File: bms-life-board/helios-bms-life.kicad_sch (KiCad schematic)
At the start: 66 parts, among them J1 Debug, J2 Output, J3 Outboard, J4 Battery, Q1 NMOS, Q2 SSM3J332R, U1 TPSM861253, U2 STM32L011F4Ux, U3 TPS22811, U4 TPS563207s, U5 BQ25306, U6 THVD1400D

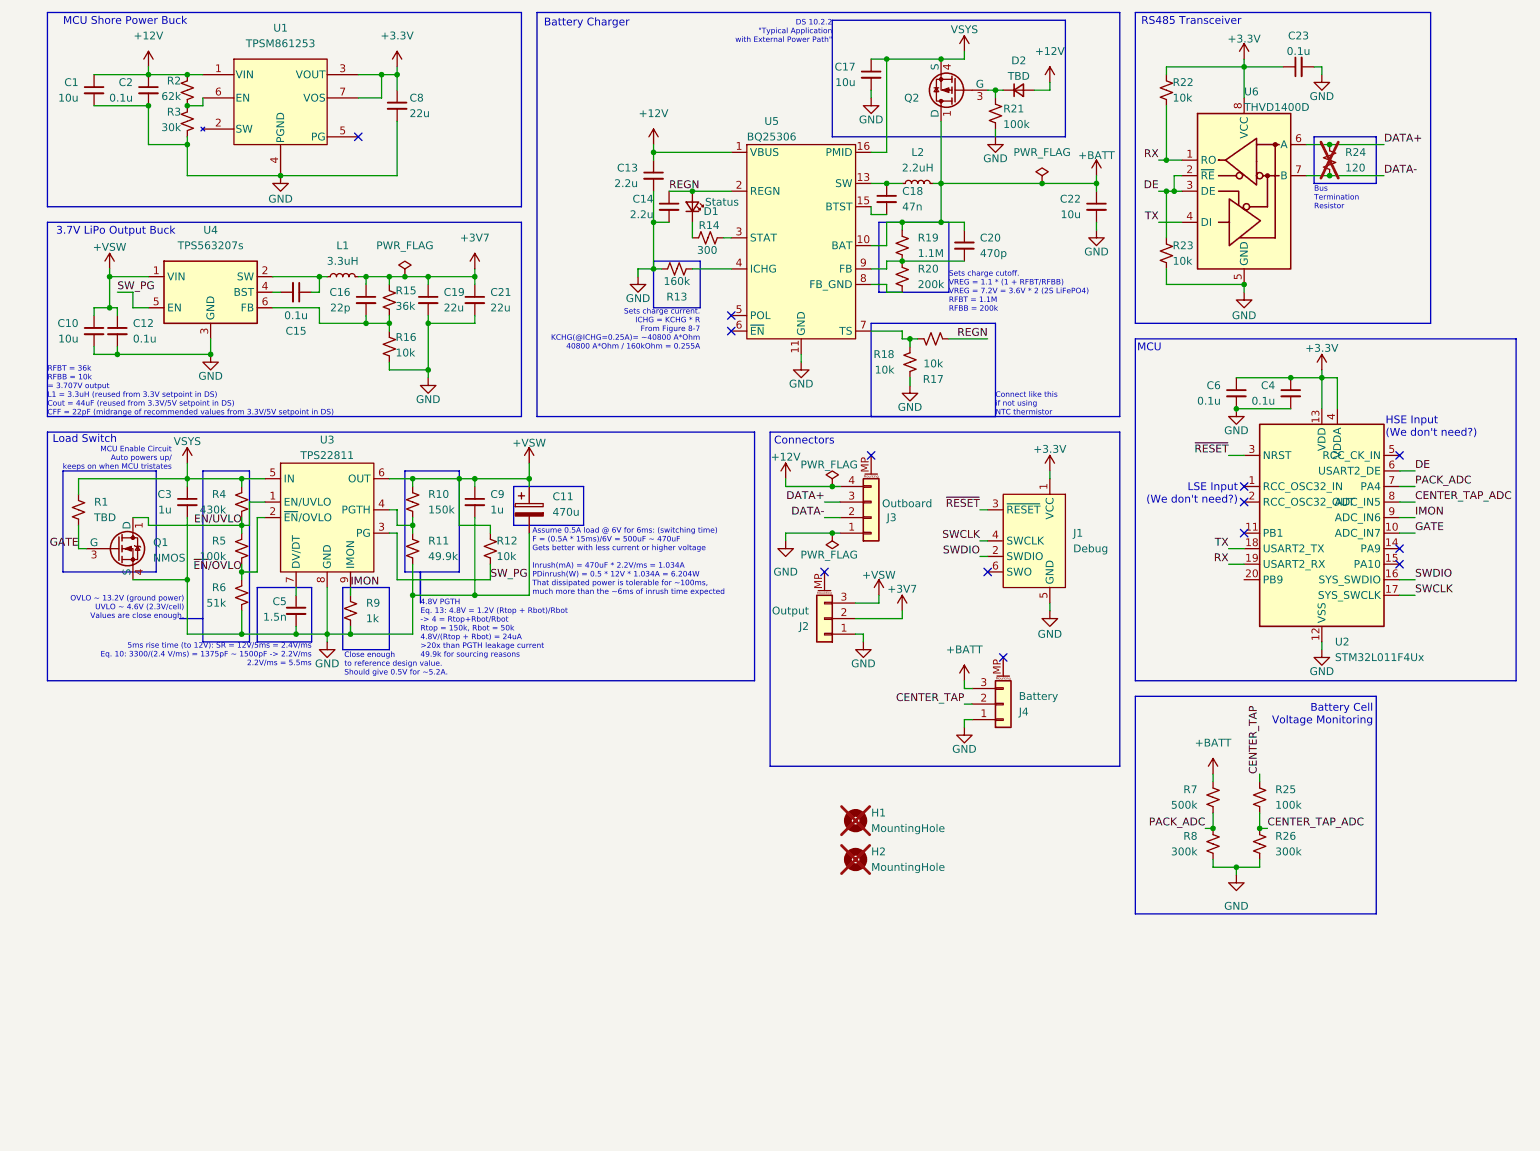
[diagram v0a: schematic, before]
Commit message: post DR LiFe board partially done, need to clean up the BoM on digikey BADDD
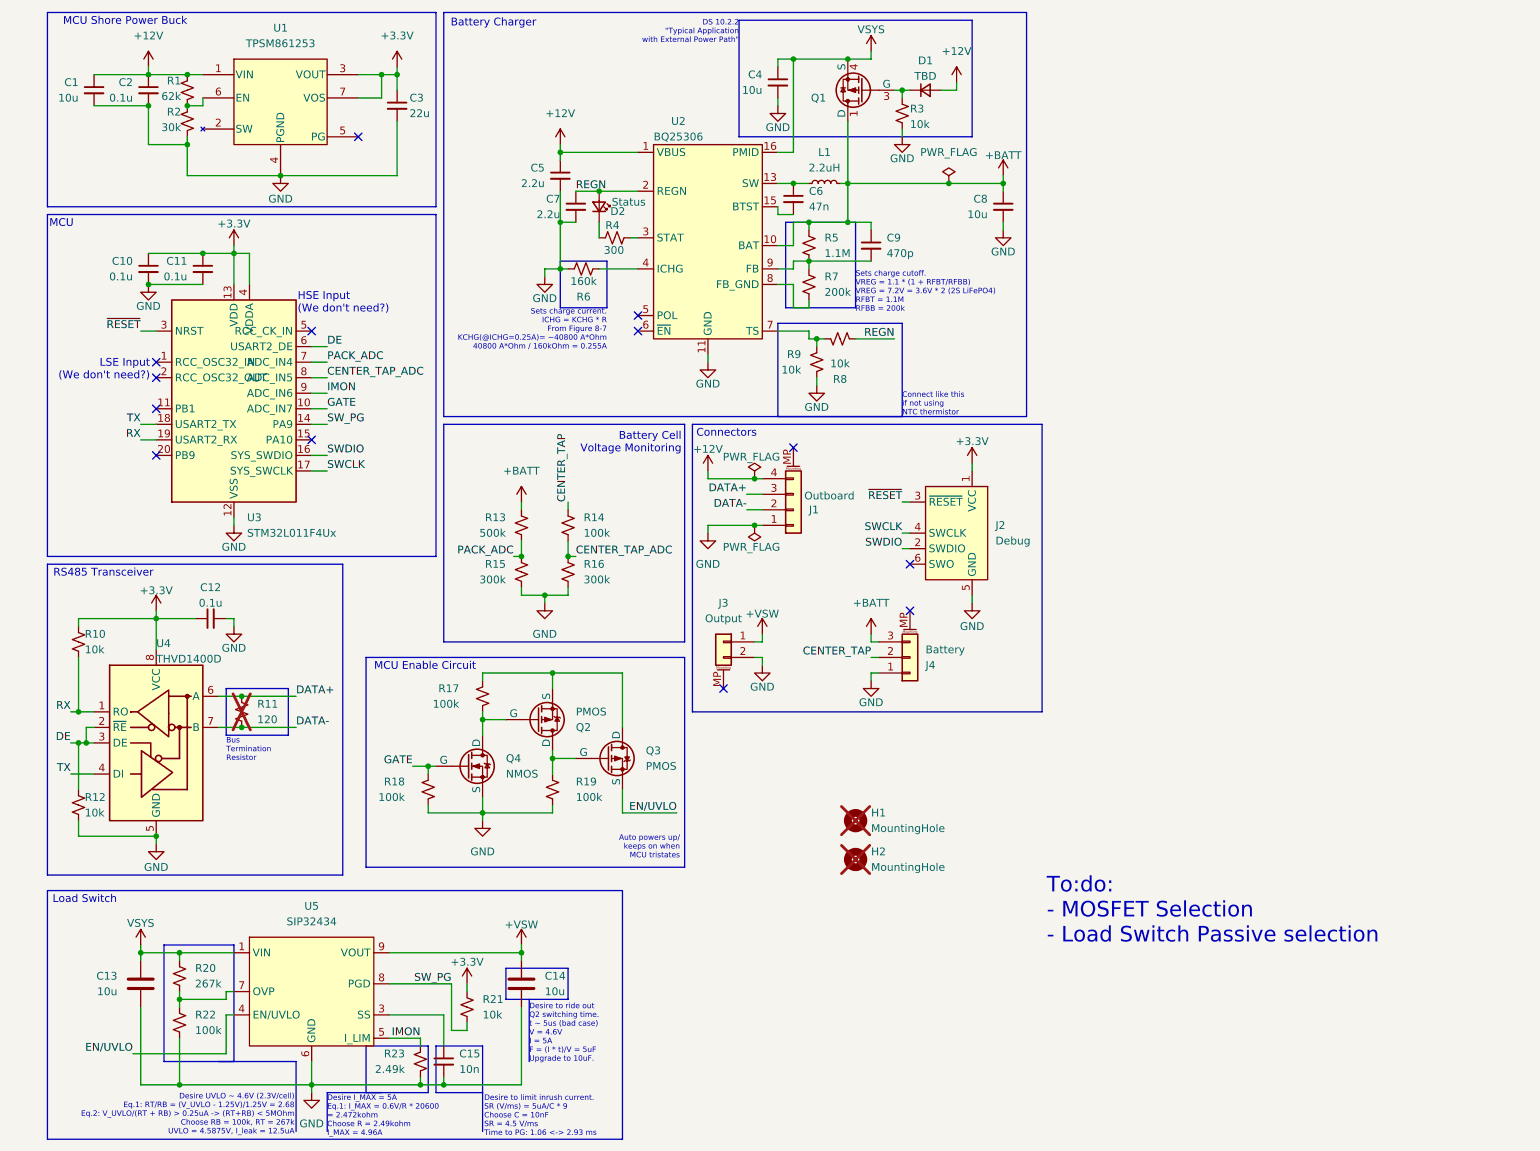
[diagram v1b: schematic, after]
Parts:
- removed C10: 10u, Capacitor_SMD:C_0603_1608Metric, symbol Device:C_Small
- removed C11: 470u, Capacitor_THT:CP_Radial_D6.3mm_P2.50mm, symbol Device:C_Polarized
- removed C12: 0.1u, Capacitor_SMD:C_0402_1005Metric, symbol Device:C_Small
- removed C16: 22p, Capacitor_SMD:C_0402_1005Metric, symbol Device:C_Small
- removed C19, C21: 22u, Capacitor_SMD:C_0603_1608Metric, symbol Device:C_Small
- removed C3, C9: 1u, Capacitor_SMD:C_0402_1005Metric, symbol Device:C_Small
- removed C5: 1.5n, Capacitor_SMD:C_0402_1005Metric, symbol Device:C_Small
- removed J2: Output, Connector_JST:JST_ZE_SM03B-ZESS-TB_1x03-1MP_P1.50mm_Horizontal, symbol Connector_Generic_MountingPin:Conn_01x03_MountingPin
- removed L1: 3.3uH, Inductor_SMD:L_1008_2520Metric, symbol Device:L_Small
- removed Q1: NMOS, Helios-BMS:SOT-1220_UDFN6B_TOS-L, symbol Helios-BMS:SSM6K388NU
- removed R1: TBD, Resistor_SMD:R_0402_1005Metric, symbol Device:R_Small_US
- removed R10: 150k, Resistor_SMD:R_0402_1005Metric, symbol Device:R_Small_US
- removed R11: 49.9k, Resistor_SMD:R_0402_1005Metric, symbol Device:R_Small_US
- removed R12, R16: 10k, Resistor_SMD:R_0402_1005Metric, symbol Device:R_Small_US
- removed R15: 36k, Resistor_SMD:R_0402_1005Metric, symbol Device:R_Small_US
- removed R4: 430k, Resistor_SMD:R_0402_1005Metric, symbol Device:R_Small_US
- removed R5: 100k, Resistor_SMD:R_0402_1005Metric, symbol Device:R_Small_US
- removed R6: 51k, Resistor_SMD:R_0402_1005Metric, symbol Device:R_Small_US
- removed R9: 1k, Resistor_SMD:R_0402_1005Metric, symbol Device:R_Small_US
- removed U3: TPS22811, Helios-BMS:TPS22811, symbol Helios-BMS:TPS22811
- removed U4: TPS563207s, Package_TO_SOT_SMD:SOT-563, symbol Regulator_Switching:TPS563206
- added C13, C14: 10u, Capacitor_SMD:C_0603_1608Metric, symbol Device:C
- added J3: Output, Connector_JST:JST_ZE_SM02B-ZESS-TB_1x02-1MP_P1.50mm_Horizontal, symbol Connector_Generic_MountingPin:Conn_01x02_MountingPin
- added Q2, Q3: PMOS, symbol Simulation_SPICE:PMOS
- added Q4: NMOS, symbol Simulation_SPICE:NMOS
- added R17, R18, R19, R22: 100k, Resistor_SMD:R_0402_1005Metric, symbol Device:R_Small_US
- added R20: 267k, Resistor_SMD:R_0402_1005Metric, symbol Device:R_Small_US
- added R21: 10k, Resistor_SMD:R_0402_1005Metric, symbol Device:R_Small_US
- added R23: 2.49k, Resistor_SMD:R_0402_1005Metric, symbol Device:R_Small_US
- added U5: SIP32434, Package_DFN_QFN:Maxim_TDFN-10-1EP_3x3mm_P0.5mm_EP1.58x2.35mm, symbol Helios-BMS:SIP32434
- C15: value 0.1u -> 10n
- R3: renamed from R21; value 100k -> 10k
- renumbered C6 to C10, C4 to C11, C23 to C12, C8 to C3, C17 to C4, C13 to C5, C18 to C6, C14 to C7, C22 to C8, C20 to C9, D2 to D1, D1 to D2, J3 to J1, J1 to J2, L2 to L1, Q2 to Q1, R2 to R1, R22 to R10, R24 to R11, R23 to R12, R7 to R13, R25 to R14, R8 to R15, R26 to R16, R3 to R2, R14 to R4, R19 to R5, R13 to R6, R20 to R7, R17 to R8, R18 to R9, U5 to U2, U2 to U3, U6 to U4
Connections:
- net +3.3V: now also R21.2
- net +VSW: now also C14.1, J3.1 (Pin_1), U5.10 (VOUT), U5.9 (VOUT)
- net EN/UVLO: now also Q3.3 (S), U5.4 (EN/UVLO)
- net GATE: now also Q4.2 (G), R18.1
- net GND: now also C15.2, C13.2, C14.2, J3.2 (Pin_2), Q4.3 (S), R18.2, R19.2, R22.1, R23.1, U5.11 (GND), U5.6 (GND)
- net IMON: now also R23.2, U5.5 (I_LIM)
- net SW_PG: now also U3.14 (PA9), R21.1, U5.8 (PGD)
- net at C15.1: now also U5.3 (SS)
- net VSYS renamed VIN
- net VIN: now also C13.1, R20.2, U5.1 (VIN), U5.2 (VIN)
- new net: Q2.1 (D), Q3.2 (G), R19.1
- new net: Q2.2 (G), Q4.1 (D), R17.2
- new net: Q2.3 (S), Q3.1 (D), R17.1
- new net: R20.1, R22.2, U5.7 (OVP)
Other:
- note added: "Auto powers up/ keeps on when MCU tristates"
- note added: "Desire I_MAX = 5A Eq.1: I_MAX = 0.6V/R * 20600 = 2.472kohm Choose R = 2.49kohm I_MAX = 4.96A"
- note added: "Desire UVLO ~ 4.6V (2.3V/cell) Eq.1: RT/RB = (V_UVLO - 1.25V)/1.25V = 2.68 Eq.2: V_UVLO/(RT + RB) > 0.25uA -> (RT+RB) < 5MOhm Choose RB = 100k, RT = 267k UVLO = 4.5875V, I_leak = 12.5uA"
- note added: "Desire to limit inrush current. SR (V/ms) = 5uA/C * 9 Choose C = 10nF SR = 4.5 V/ms Time to PG: 1.06 <-> 2.93 ms"
- note added: "Desire to ride out Q2 switching time. t ~ 5us (bad case) V = 4.6V I = 5A F = (I * t)/V = 5uF Upgrade to 10uF."
- note added: "MCU Enable Circuit"
- note added: "To:do: - MOSFET Selection - Load Switch Passive selection"
- note removed: "3.7V LiPo Output Buck"
- note removed: "4.8V PGTH Eq. 13: 4.8V = 1.2V (Rtop + Rbot)/Rbot -> 4 = Rtop+Rbot/Rbot Rtop = 150k, Rbot = 50k 4.8V/(Rtop + Rbot) = 24uA >20x than PGTH leakage current 49.9k for sourcing reasons"
- note removed: "5ms rise time (to 12V): SR = 12V/5ms = 2.4V/ms Eq. 10: 3300/(2.4 V/ms) = 1375pF ~ 1500pF -> 2.2V/ms 2.2V/ms = 5.5ms"
- note removed: "Assume 0.5A load @ 6V for 6ms: (switching time) F = (0.5A * 15ms)/6V = 500uF ~ 470uF Gets better with less current or higher voltage Inrush(mA) = 470uF * 2.2V/ms = 1.034A PDinrush(W) = 0.5 * 12V * 1.034A = 6.204W That dissipated power is tolerable for ~100ms, much more than the ~6ms of inrush time expected"
- note removed: "Close enough to reference design value. Should give 0.5V for ~5.2A."
- note removed: "MCU Enable Circuit Auto powers up/ keeps on when MCU tristates"
- note removed: "OVLO ~ 13.2V (ground power) UVLO ~ 4.6V (2.3V/cell) Values are close enough."
- note removed: "RFBT = 36k RFBB = 10k = 3.707V output L1 = 3.3uH (reused from 3.3V setpoint in DS) Cout = 44uF (reused from 3.3V/5V setpoint in DS) CFF = 22pF (midrange of recommended values from 3.3V/5V setpoint in DS)"
- moved on the sheet: C10, C11, C12, C4, C5, C6, C7, C8, C9, D1, D2, J1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

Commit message: LiFe board done
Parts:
- removed Q2, Q3: PMOS, symbol Simulation_SPICE:PMOS
- removed Q4: NMOS, symbol Simulation_SPICE:NMOS
- added Q2: Q_Dual_NMOS_PMOS_S1G1D2S2G2D1, Package_TO_SOT_SMD:SOT-666, symbol Helios-BMS:Q_Dual_NMOS_PMOS_S1G1D2S2G2D1
- added Q3: PMOS, Package_TO_SOT_SMD:SOT-723, symbol Transistor_FET:Q_PMOS_GSD
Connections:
- net +12V: now also R17.1, Q2.4 (S), Q3.3 (D)
- net +VSW: now also J3.2 (Pin_2); no longer J3.1 (Pin_1)
- net EN/UVLO: now also Q3.2 (S)
- net GATE: now also U3.9 (PA6), Q2.2 (G); no longer U3.10 (PA7)
- net GND: now also J3.1 (Pin_1), Q2.1 (S); no longer J3.2 (Pin_2)
- net IMON: now also U3.10 (PA7); no longer U3.9 (PA6)
- net at R19.1: now also Q2.3 (D), Q3.1 (G)
- net at R17.2: now also Q2.5 (G), Q2.6 (D)
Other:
- moved on the sheet: H1, H2, J3
